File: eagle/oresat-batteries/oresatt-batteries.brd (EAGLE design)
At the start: 94 x 93.5 mm, 62 parts, among them U1 TCAN330, U2 STM32F042K6, X1 16MHz

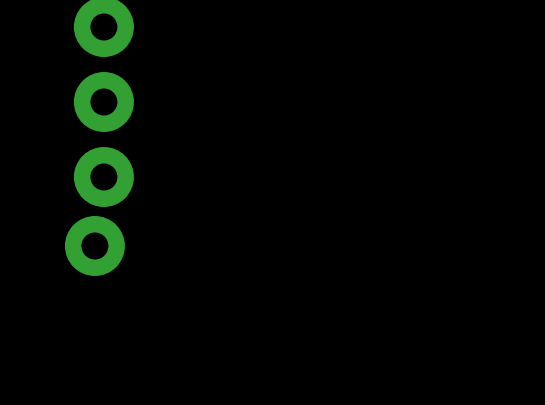
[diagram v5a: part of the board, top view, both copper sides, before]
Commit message: Named missing NETS
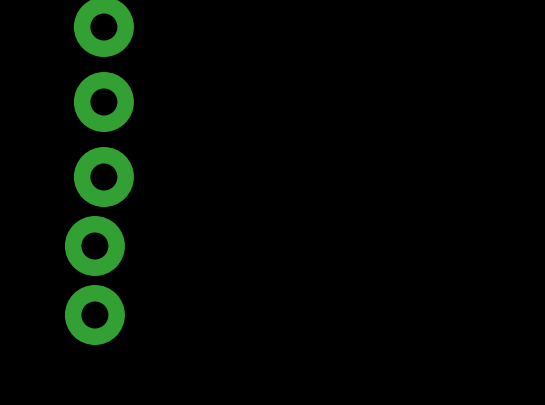
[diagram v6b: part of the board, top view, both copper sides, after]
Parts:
- added U$27: TP, oresat-batteries:2MM_TP
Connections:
- net N$10 renamed DIG_IO2
- net N$11 renamed DIG_IO3
- net N$14 renamed HEAT
- net N$3 renamed IO0
- net N$31 renamed NRESET
- net N$5 renamed CANH
- net N$6 renamed CANL
- net N$7 renamed ROSC
- net N$8 renamed SYS_EN
- net N$9 renamed DIG_IO1
- new net PA8: U2.18
- net STM_DEBUG: now also U2.6; no longer U2.10
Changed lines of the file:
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@@
 <element name="U$25" library="oresat-batteries" package="2MM_TP" value="TP" x="-21.5" y="-36.5"/>
 <element name="U$26" library="oresat-batteries" package="2MM_TP" value="TP" x="-21.8" y="-38.8"/>
+<element name="U$27" library="oresat-batteries" package="2MM_TP" value="TP" x="-21.8" y="-41.1"/>
 </elements>
 <signals>
@@
 <wire x1="11.65" y1="70" x2="21.35" y2="81.93" width="0" layer="19" extent="1-1"/>
 </signal>
-<signal name="N$7">
+<signal name="ROSC">
 <contactref element="U$5" pad="2"/>
 <contactref element="R4" pad="2"/>
@@
 </signal>
 <signal name="STM_DEBUG">
-<contactref element="U2" pad="10"/>
 <contactref element="CF2" pad="8"/>
-<wire x1="4.25" y1="66.5" x2="15" y2="58.25" width="0" layer="19" extent="1-1"/>
+<contactref element="U2" pad="6"/>
+<wire x1="4.25" y1="66.5" x2="12.75" y2="61.3" width="0" layer="19" extent="1-1"/>
 </signal>
 <signal name="CAN_LSTN">
@@
 <wire x1="4.25" y1="60.5" x2="21.25" y2="64.5" width="0" layer="19" extent="1-1"/>
 </signal>
-<signal name="N$31">
+<signal name="NRESET">
 <contactref element="CF2" pad="3"/>
 <contactref element="U2" pad="4"/>
@@
 <wire x1="15.5" y1="47.4" x2="9.435" y2="86.96" width="0" layer="19" extent="1-1"/>
 </signal>
-<signal name="N$3">
+<signal name="IO0">
 <contactref element="U$5" pad="1"/>
 <contactref element="R10" pad="1"/>
@@
 <wire x1="23.15" y1="57" x2="29.35" y2="68.5" width="0" layer="19" extent="1-1"/>
 </signal>
-<signal name="N$5">
+<signal name="CANH">
 <contactref element="U1" pad="7"/>
 <contactref element="CF1" pad="P$4"/>
@@
 <wire x1="7.85" y1="-16.27" x2="7.85" y2="-13.73" width="0" layer="19" extent="1-1"/>
 </signal>
-<signal name="N$6">
+<signal name="CANL">
 <contactref element="U1" pad="6"/>
 <contactref element="CF1" pad="P$5"/>
@@
 <wire x1="-2.525" y1="-3.435" x2="26.66" y2="76.825" width="0" layer="19" extent="1-1"/>
 </signal>
-<signal name="N$8">
+<signal name="SYS_EN">
 <contactref element="U2" pad="14"/>
 <contactref element="U$1" pad="16"/>
 <wire x1="18.2" y1="58.25" x2="22.85" y2="81.93" width="0" layer="19" extent="1-1"/>
 </signal>
-<signal name="N$9">
+<signal name="DIG_IO1">
 <contactref element="U$1" pad="5"/>
 <contactref element="U2" pad="15"/>
 <wire x1="19" y1="58.25" x2="20" y2="79.08" width="0" layer="19" extent="1-1"/>
 </signal>
-<signal name="N$10">
+<signal name="DIG_IO2">
 <contactref element="U$1" pad="3"/>
 <contactref element="U2" pad="26"/>
 <wire x1="19" y1="66.75" x2="20" y2="80.08" width="0" layer="19" extent="1-1"/>
 </signal>
-<signal name="N$11">
+<signal name="DIG_IO3">
 <contactref element="U$1" pad="2"/>
 <contactref element="U2" pad="27"/>
@@
 <wire x1="-22.475" y1="-20.935" x2="-21.825" y2="-20.935" width="0" layer="19" extent="1-1"/>
 </signal>
-<signal name="N$14">
+<signal name="HEAT">
 <contactref element="U2" pad="7"/>
 <contactref element="U$20" pad="P$4"/>
@@
 <wire x1="-7.025" y1="-3.435" x2="27.16" y2="76.825" width="0" layer="19" extent="1-1"/>
 </signal>
+<signal name="PA8">
+<contactref element="U2" pad="18"/>
+</signal>
 </signals>

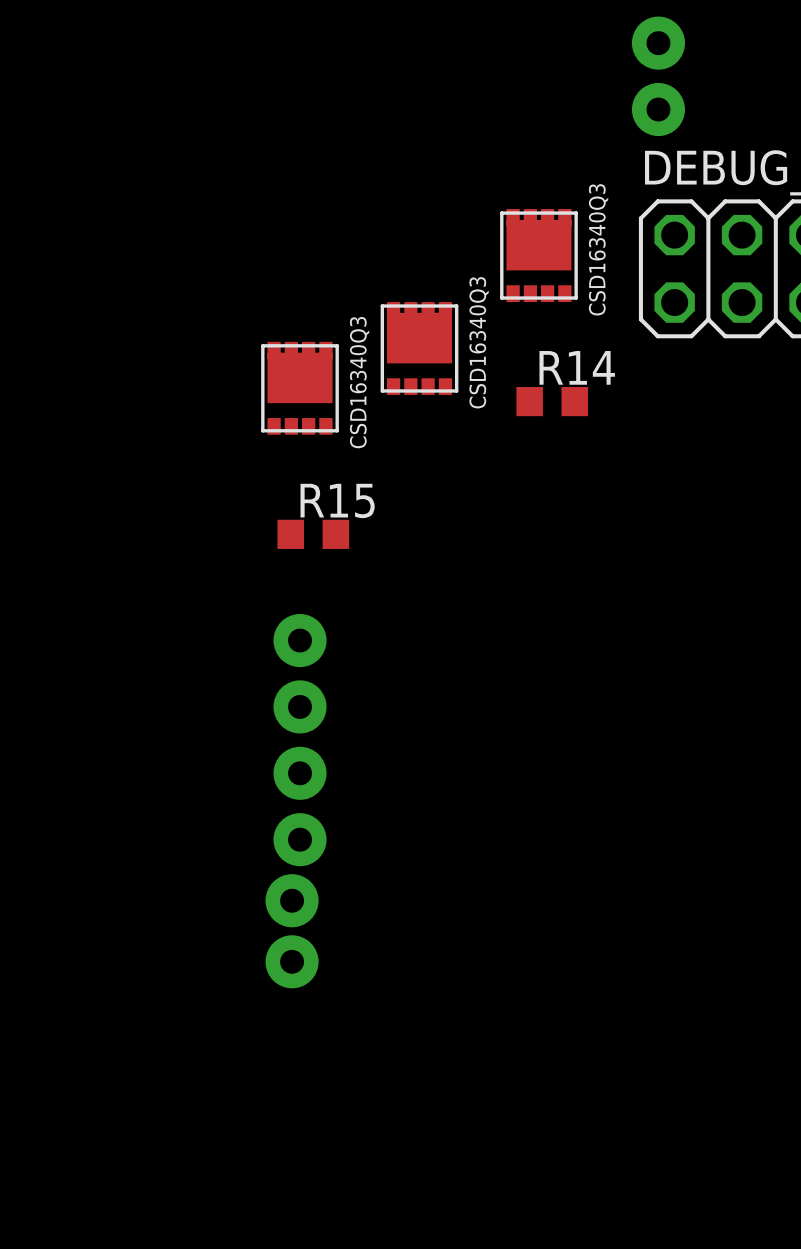
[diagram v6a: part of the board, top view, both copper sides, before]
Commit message: Replaced Shutdown with new circuitry that will actually work... maybe.
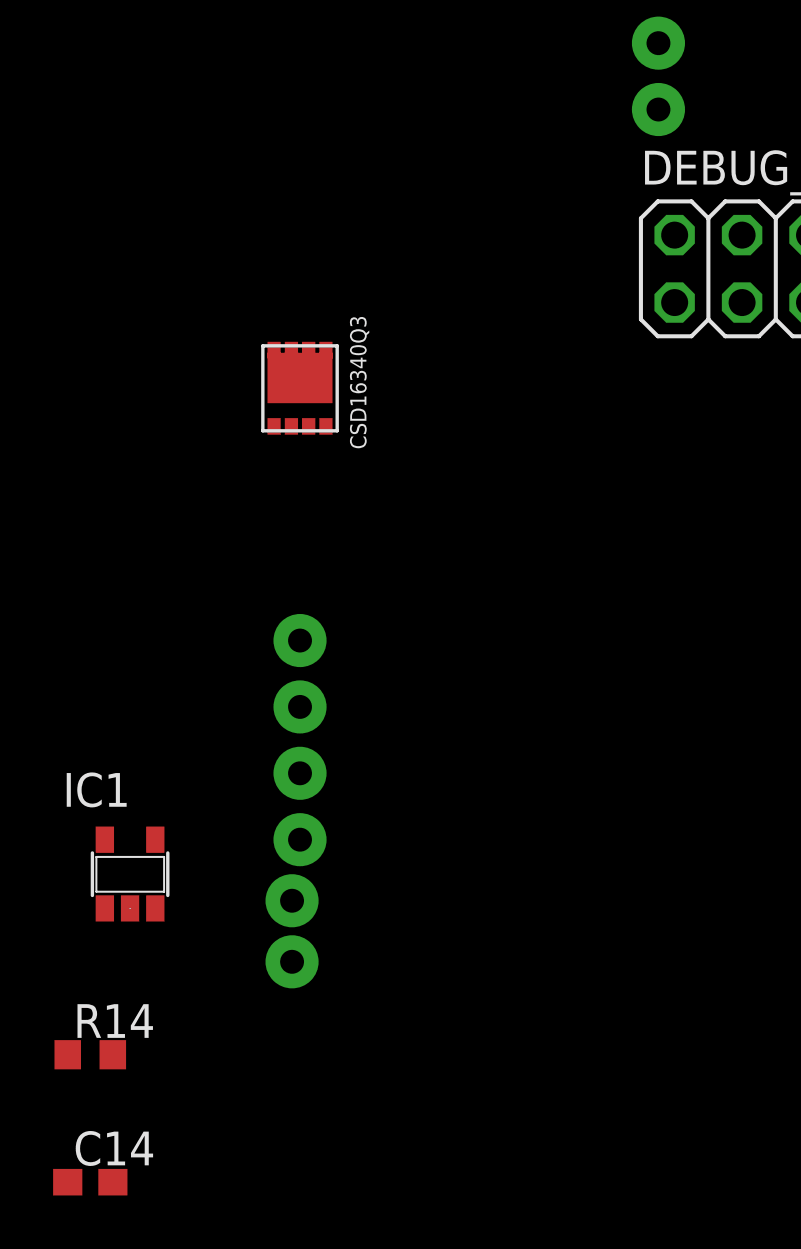
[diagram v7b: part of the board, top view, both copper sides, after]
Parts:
- removed R15: 200k, rcl:R0603
- removed U$18, U$19: CSD16340Q3, oresat-batteries:Q3
- added C14: (no value), rcl:C0603
- added IC1: 74AHC1G08DBV, 74xx-little-us:SOT23-5
- R14: value 20k -> 2.2k
- R6: value (none) -> 2.2k
- R7: value (none) -> ?
- moved R14 30.1 mm to (-29.4, -44.6)
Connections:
- removed net BATTHICUT: U$19.P$5, U$19.P$6, U$19.P$7, U$19.P$8, U$19.P$9, U$3.POS
- removed net BQKILL: R6.2, U$18.P$5, U$18.P$6, U$18.P$7, U$18.P$8, U$18.P$9, U$2.4
- removed net DOUT: U$14.P$4, U$2.3
- removed net SHORTBAR: CF1.P$6, R14.1, R15.1, U$18.P$4, U$19.P$4
- new net N$3: IC1.4, U$14.P$4
- new net N$5: IC1.2, U$2.3
- new net N$6: C14.1, IC1.5, R14.1
- net BQBAT: now also CF1.P$6, IC1.1, R14.2
- net GND: now also C14.2, IC1.3, R3.2, R6.2, U$5.6; no longer R15.2, U$18.P$1, U$18.P$2, U$18.P$3
- net STC_CG: now also U$2.4; no longer R3.2, U$5.6
- net VBATT+: now also U$3.POS; no longer R14.2, U$19.P$1, U$19.P$2, U$19.P$3
